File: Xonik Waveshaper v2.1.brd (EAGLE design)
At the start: 63.5 x 28.8 mm, 90 parts, among them IC1 TL074D, IC2 TL074D, IC3 TL074D, IC4 TL072D, IC5 4013D, T1 2n3904

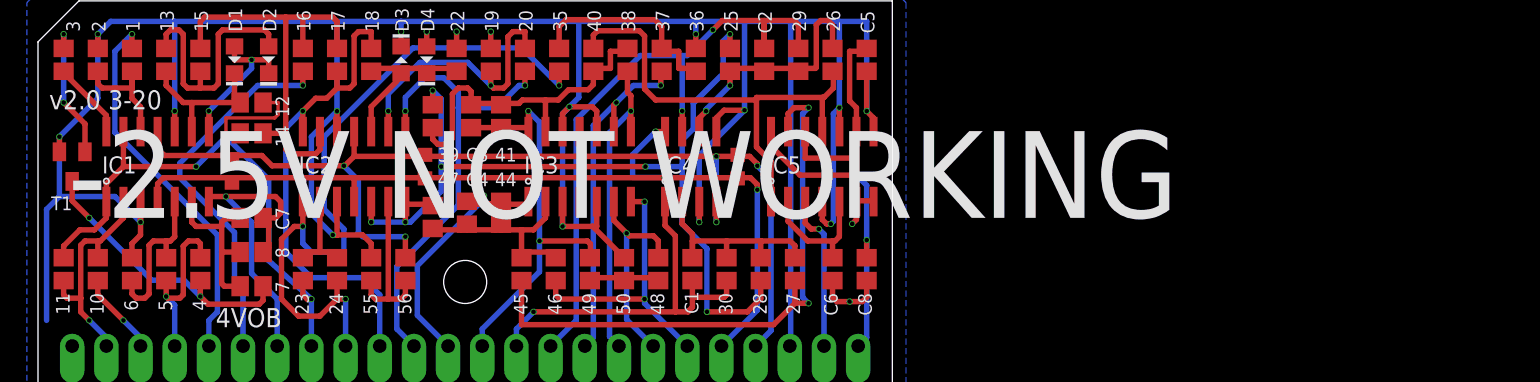
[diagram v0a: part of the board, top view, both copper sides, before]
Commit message: v2.1 - fixed serious bug, had mixed up + and - on -2.5v generator op amp
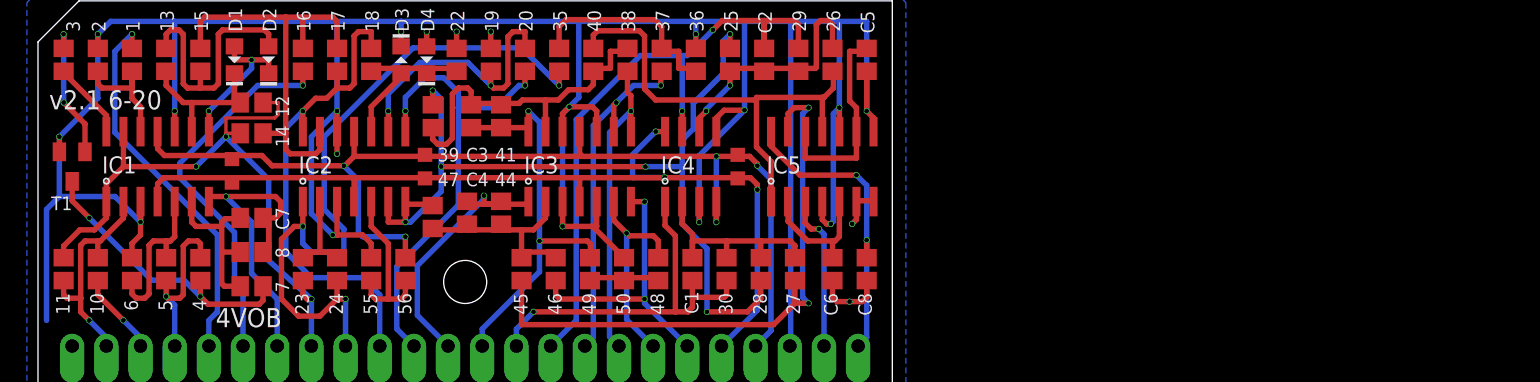
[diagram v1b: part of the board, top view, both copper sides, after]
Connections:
- net -2.5V: now also IC2.6; no longer IC2.5
- net N$33: now also IC2.5; no longer IC2.6
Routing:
- net -2.5V: track 67.8 -> 66.5 mm, vias 7 -> 6
- net N$33: track 12.2 -> 12.7 mm
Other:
- board text added: "v2.1 6-20"
- board text removed: "-2.5V NOT WORKING"
- board text removed: "v2.0 3-20"
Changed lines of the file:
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@@
 <text x="58.1025" y="5.3975" size="1.016" layer="26" rot="MR90">Timer in</text>
 <text x="60.325" y="5.3975" size="1.016" layer="26" rot="MR90">+5V</text>
-<text x="0.8255" y="20.7645" size="1.4224" layer="25" font="vector">v2.0 3-20</text>
+<text x="0.8255" y="20.7645" size="1.4224" layer="25" font="vector">v2.1 6-20</text>
 <text x="7.5565" y="26.543" size="1.016" layer="25" rot="R90">1</text>
 <text x="5.0165" y="26.543" size="1.016" layer="25" rot="R90">2</text>
@@
 <text x="61.722" y="25.527" size="1.778" layer="26" font="vector" rot="MR0">Waveshaper</text>
 <text x="13.208" y="4.572" size="1.4224" layer="25" font="vector">4VOB</text>
-<text x="2.2225" y="12.7" size="6.4516" layer="25">-2.5V NOT WORKING</text>
 </plain>
 <attributes>
@@
 <contactref element="39" pad="2"/>
 <contactref element="47" pad="2"/>
-<contactref element="IC2" pad="5"/>
 <contactref element="IC2" pad="7"/>
 <via x="29.972" y="16.51" extent="1-16" drill="0.3302"/>
@@
 <wire x1="27.305" y1="13.91" x2="27.499" y2="13.716" width="0.4064" layer="1"/>
 <wire x1="29.337" y1="21.1065" x2="29.337" y2="22.1615" width="0.4064" layer="1"/>
-<wire x1="24.765" y1="13.91" x2="24.765" y2="12.3825" width="0.4064" layer="1"/>
-<via x="24.765" y="12.3825" extent="1-16" drill="0.3302"/>
-<wire x1="24.765" y1="12.3825" x2="27.305" y2="12.3825" width="0.4064" layer="16"/>
 <wire x1="47.879" y1="16.51" x2="47.879" y2="18.4785" width="0.4064" layer="16"/>
 <wire x1="47.879" y1="18.4785" x2="48.7045" y2="19.304" width="0.4064" layer="16"/>
@@
 <wire x1="48.7045" y1="21.209" x2="48.7045" y2="19.304" width="0.4064" layer="16"/>
 <wire x1="47.879" y1="16.51" x2="45.1485" y2="16.51" width="0.4064" layer="16"/>
+<contactref element="IC2" pad="6"/>
+<wire x1="26.035" y1="13.91" x2="26.035" y2="12.3825" width="0.4064" layer="1"/>
+<wire x1="26.035" y1="12.3825" x2="27.305" y2="12.3825" width="0.4064" layer="1"/>
 </signal>
 <signal name="N$20">
@@
 <contactref element="55" pad="1"/>
 <contactref element="56" pad="2"/>
-<contactref element="IC2" pad="6"/>
 <wire x1="24.765" y1="8.04" x2="24.765" y2="6.985" width="0.4064" layer="1"/>
 <wire x1="24.765" y1="6.985" x2="25.0825" y2="6.6675" width="0.4064" layer="1"/>
 <wire x1="25.0825" y1="6.6675" x2="26.035" y2="6.6675" width="0.4064" layer="1"/>
-<wire x1="26.035" y1="13.91" x2="26.035" y2="6.6675" width="0.4064" layer="1"/>
 <wire x1="27.305" y1="8.04" x2="27.305" y2="6.985" width="0.4064" layer="1"/>
 <wire x1="27.305" y1="6.985" x2="26.9875" y2="6.6675" width="0.4064" layer="1"/>
 <wire x1="26.9875" y1="6.6675" x2="26.035" y2="6.6675" width="0.4064" layer="1"/>
+<contactref element="IC2" pad="5"/>
+<wire x1="24.765" y1="13.91" x2="24.765" y2="12.065" width="0.4064" layer="1"/>
+<wire x1="24.765" y1="12.065" x2="26.035" y2="10.795" width="0.4064" layer="1"/>
+<wire x1="26.035" y1="10.795" x2="26.035" y2="6.6675" width="0.4064" layer="1"/>
 </signal>
 <signal name="N$31">

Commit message: Replaced 1.5k R19 with 1.2k for a sine closer to +/-5v
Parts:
- 19: value 1k5 -> 1k2
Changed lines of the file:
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@@
 <attribute name="VALUE" x="27.051" y="23.6855" size="1.27" layer="27" rot="R90"/>
 </element>
-<element name="19" library="resistor" package="R0805" value="1k5" x="33.655" y="24.4475" smashed="yes" rot="R90">
+<element name="19" library="resistor" package="R0805" value="1k2" x="33.655" y="24.4475" smashed="yes" rot="R90">
 <attribute name="VALUE" x="35.941" y="23.6855" size="1.27" layer="27" rot="R90"/>
 </element>

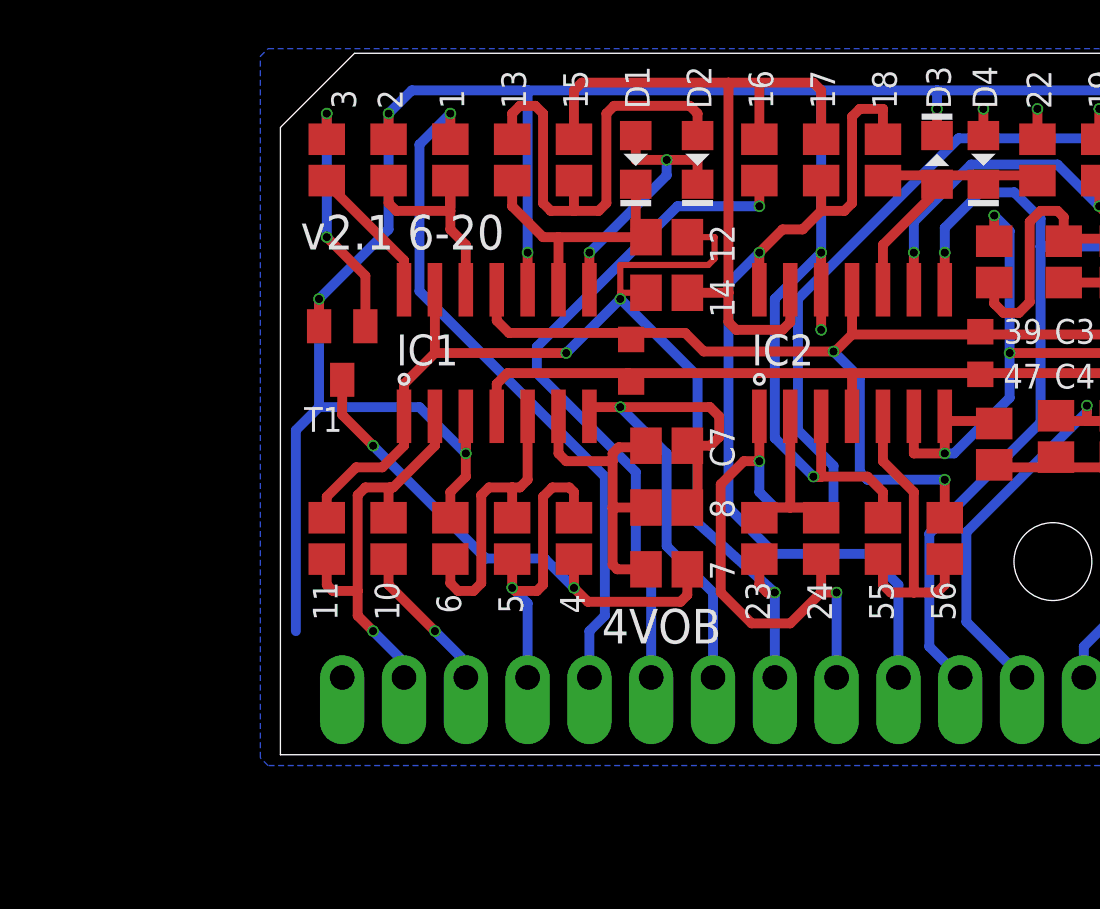
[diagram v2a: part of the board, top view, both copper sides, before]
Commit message: will remove resistor divider
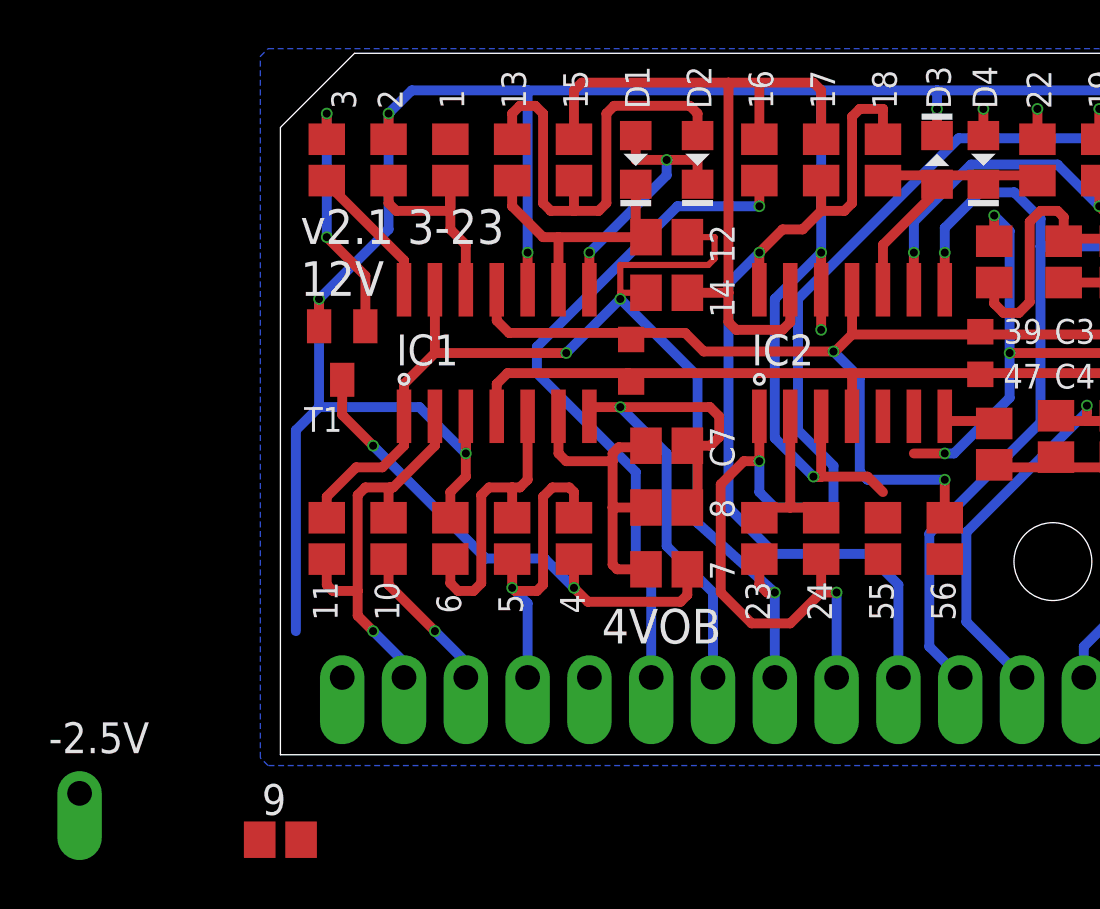
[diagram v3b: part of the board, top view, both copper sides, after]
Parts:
- added -2.5V: (no value), joakim:SIP-PIN01-1J
- added 9: 50k, resistor:R0805
- 55: value 20k -> 100k
- 56: value 100k -> 240k
- renumbered +15V to +12V, -15V to -12V
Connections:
- net +15V renamed +12V
- net -15V renamed -12V
- removed net PW_CV: 1.2, PW_CV.1
- new net N$25: 1.2, 55.2, IC2.7
- new net N$8: 55.1, 56.2, 9.1, IC2.6
- net -2.5V: now also -2.5V.1; no longer IC2.6, IC2.7
- net GND: now also IC2.5; no longer 55.2
- net N$33: now also 9.2, PW_CV.1; no longer 55.1, 56.2, IC2.5
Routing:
- net PW_CV: track 28.2 -> 0.00 mm, vias 1 -> 0
- net N$33: track 12.7 -> 0.00 mm
- net -2.5V: track 66.5 -> 63.2 mm
- net GND: track 255.3 -> 254.3 mm
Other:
- board text added: "v2.1 3-23 12V"
- board text removed: "v2.1 6-20"

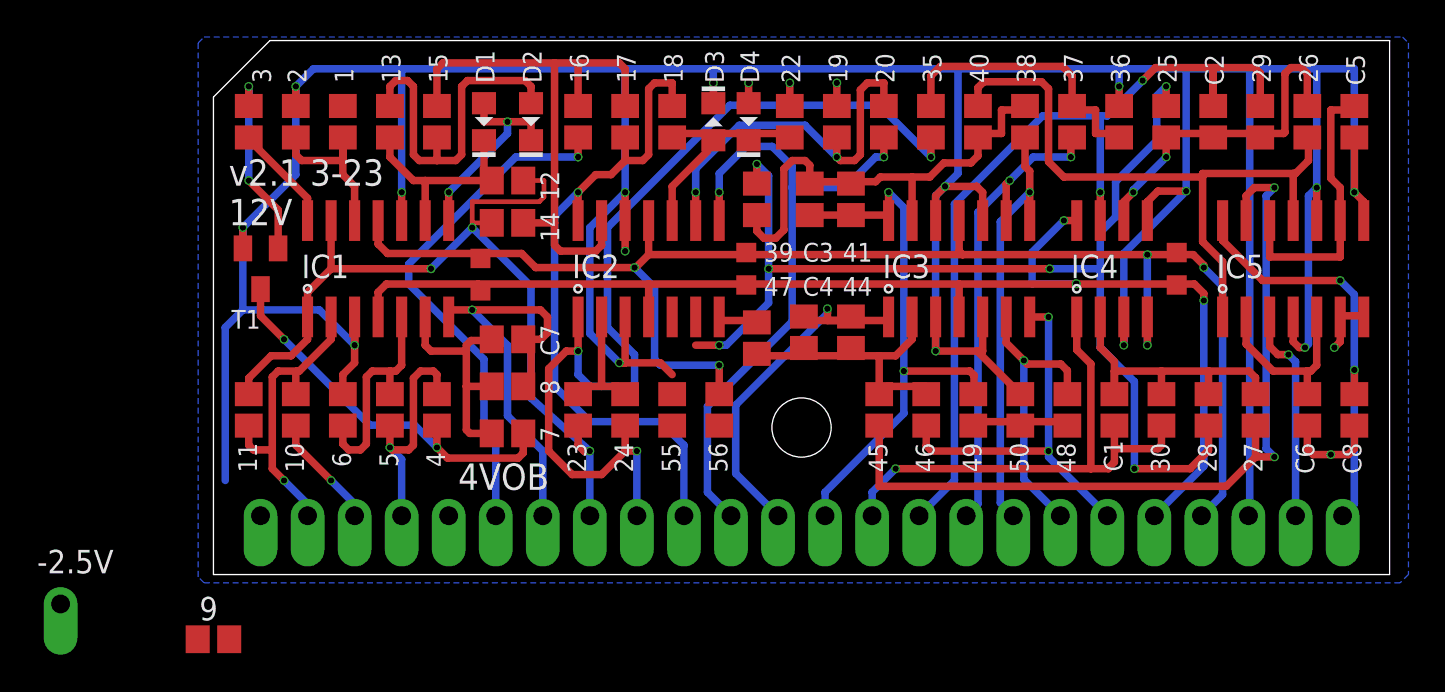
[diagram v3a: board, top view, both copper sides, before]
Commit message: Split connector into 19p + 5p to use available from JLCPB
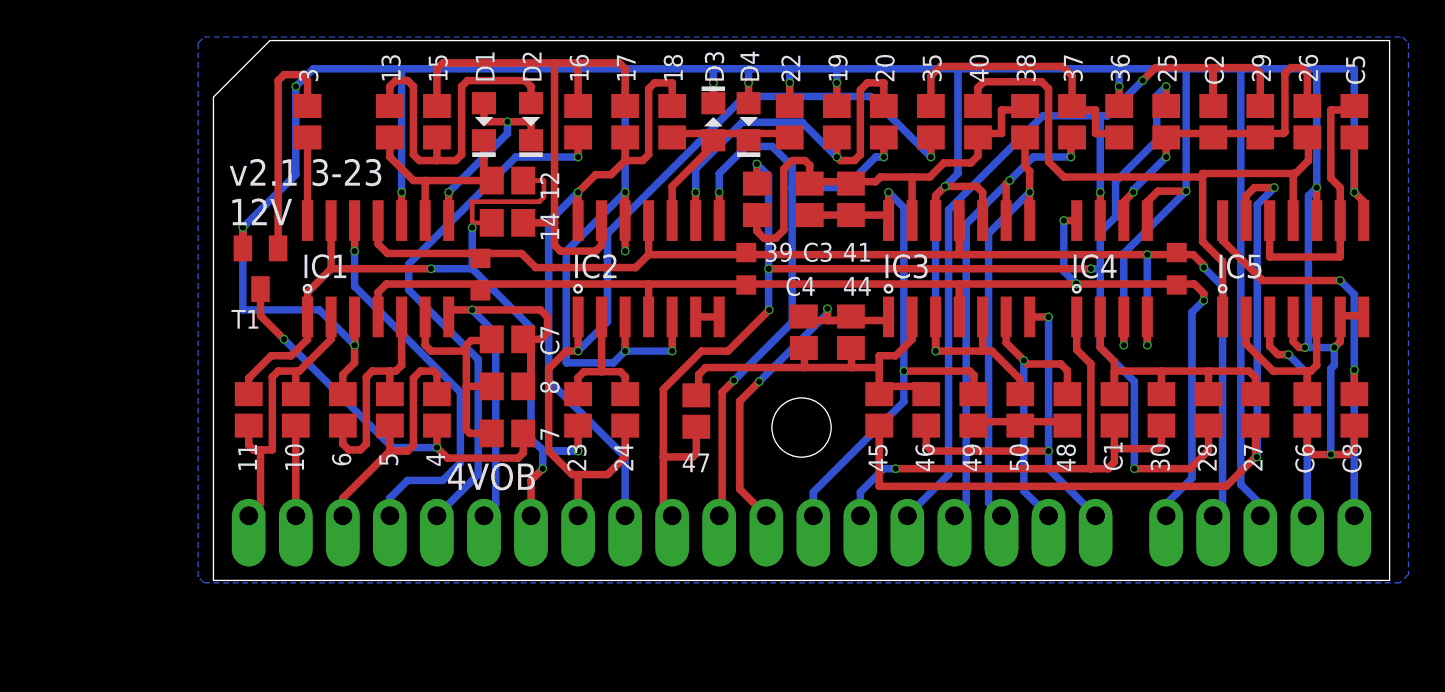
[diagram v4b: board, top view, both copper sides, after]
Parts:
- removed 1: 10k, resistor:R0805
- removed 2: 82k, resistor:R0805
- removed 55: 100k, resistor:R0805
- removed 56: 240k, resistor:R0805
- removed 9: 50k, resistor:R0805
- removed GND27: (no value), joakim:SIP-PIN01-1J
- C3, C4: value ?pF -> 30pF
- moved -2.5V 33.4 mm to (24.8, 3.17)
- moved 47 5.12 mm to (26.1, 8.83), turned to 270 degrees
- moved INV_SAW 3.18 mm to (17.1, 3.17)
- moved PULSE 3.18 mm to (14.6, 3.17)
- moved SAW 3.18 mm to (19.7, 3.17)
- moved SYMMETRY 3.18 mm to (12.1, 3.17)
- moved 3 3.17 mm to (5.08, 24.4)
- moved CENTER 3.17 mm to (1.91, 3.17)
- moved DCO_IN 3.17 mm to (4.45, 3.17)
- moved PULSE_AMP_CV 3.17 mm to (6.99, 3.17)
- moved PW_CV 3.17 mm to (9.53, 3.17)
- moved TRIANGLE 3.17 mm to (22.2, 3.17)
- moved +12V 0.64 mm to (51.4, 3.17)
- moved SUB_SAW_1 0.64 mm to (32.4, 3.17)
- moved SUB_SQR_2 0.64 mm to (34.9, 3.17)
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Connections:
- net N$38 renamed TRIANGLE
- removed net N$25: 1.2, 55.2, IC2.7
- removed net N$8: 55.1, 56.2, 9.1, IC2.6
- net -12V: no longer 56.1
- net GND: no longer 2.1
- net N$1: now also IC2.6, IC2.7; no longer 1.1, 2.2, IC1.12
- net N$33: now also IC1.12; no longer 9.2
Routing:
- net N$33: track 0.00 -> 21.0 mm, vias 0 -> 1
- net -2.5V: track 63.2 -> 74.6 mm
- net -12V: track 82.6 -> 71.7 mm, vias 5 -> 3
- net N$1: track 9.68 -> 1.27 mm
- net N$16: track 55.1 -> 47.2 mm, vias 3 -> 2
- net N$29: track 16.9 -> 23.2 mm
- net TRIANGLE: track 37.0 -> 33.7 mm
- net GND: track 254.3 -> 257.5 mm, vias 21 -> 22
- net +12V: track 70.7 -> 67.6 mm
- net N$3: track 11.1 -> 12.9 mm, vias 2 -> 0
- net N$9: track 50.1 -> 51.7 mm, vias 3 -> 4
- net N$2: track 5.80 -> 4.49 mm
- net DCO_IN: track 6.18 -> 4.86 mm, vias 1 -> 0
- net N$35: track 44.9 -> 44.0 mm
- net N$7: track 23.8 -> 23.0 mm
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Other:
- board size 63.5 x 28.8 mm -> 63.5 x 29.1 mm
- board text added: "-2.5v"
- board text removed: "55"
- board text removed: "56"

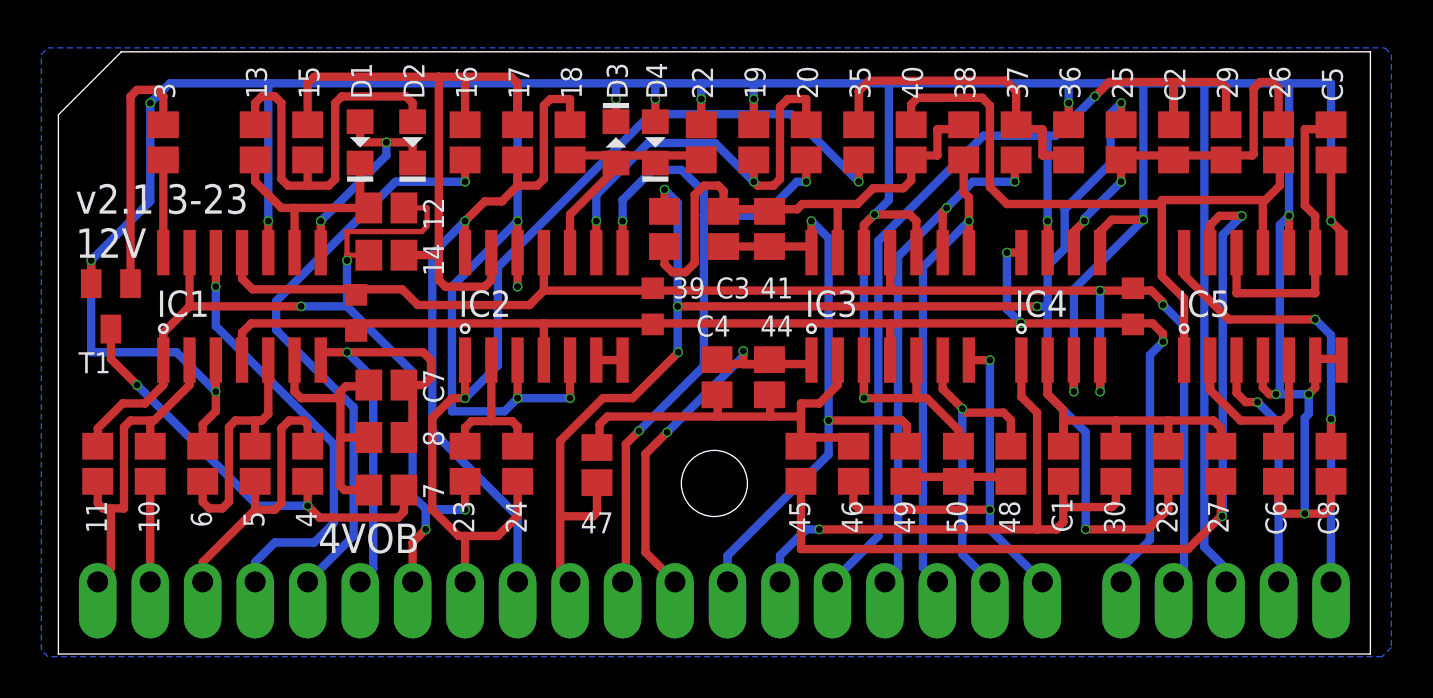
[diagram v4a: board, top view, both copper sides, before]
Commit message: Changed pin spacing to 2.54mm to still fit breadboard
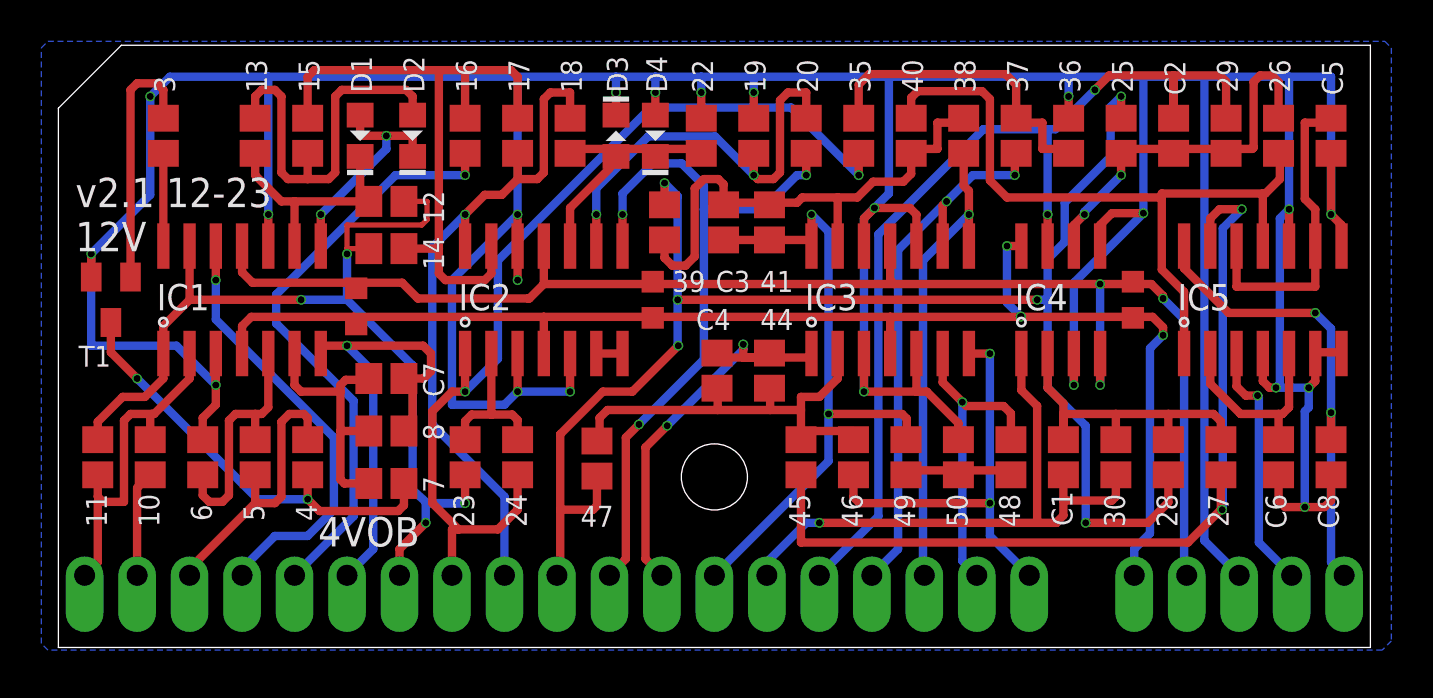
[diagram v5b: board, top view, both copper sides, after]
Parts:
- moved ST1 0.71 mm to (39.4, 3.49)
- moved ST2 0.71 mm to (41.9, 3.49)
- moved SUB_SQR_1 0.71 mm to (36.8, 3.49)
- moved -2.5V 0.71 mm to (24.1, 3.49)
- moved TRIANGLE 0.71 mm to (21.6, 3.49)
- moved PULSE_AMP_CV 0.71 mm to (6.35, 3.49)
- moved DCO_IN 0.71 mm to (3.81, 3.49)
- moved CENTER 0.71 mm to (1.27, 3.49)
- moved PULSE 0.71 mm to (14.0, 3.49)
- moved PW_CV 0.71 mm to (8.89, 3.49)
- moved SYMMETRY 0.71 mm to (11.4, 3.49)
- moved +12V 0.71 mm to (52.1, 3.49)
- moved +5V 0.71 mm to (62.2, 3.49)
- moved -12V 0.71 mm to (54.6, 3.49)
- moved DCO_TIMER 0.71 mm to (59.7, 3.49)
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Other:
- board text added: "v2.1 12-23 12V"
- board text removed: "v2.1 3-23 12V"
